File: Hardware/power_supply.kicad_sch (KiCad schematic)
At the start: 25 parts, among them J1 Conn_01x02_Pin, U1 MIC26903YJL-TR, U2 LD39200PU33R, U3 INA226AIDGSR

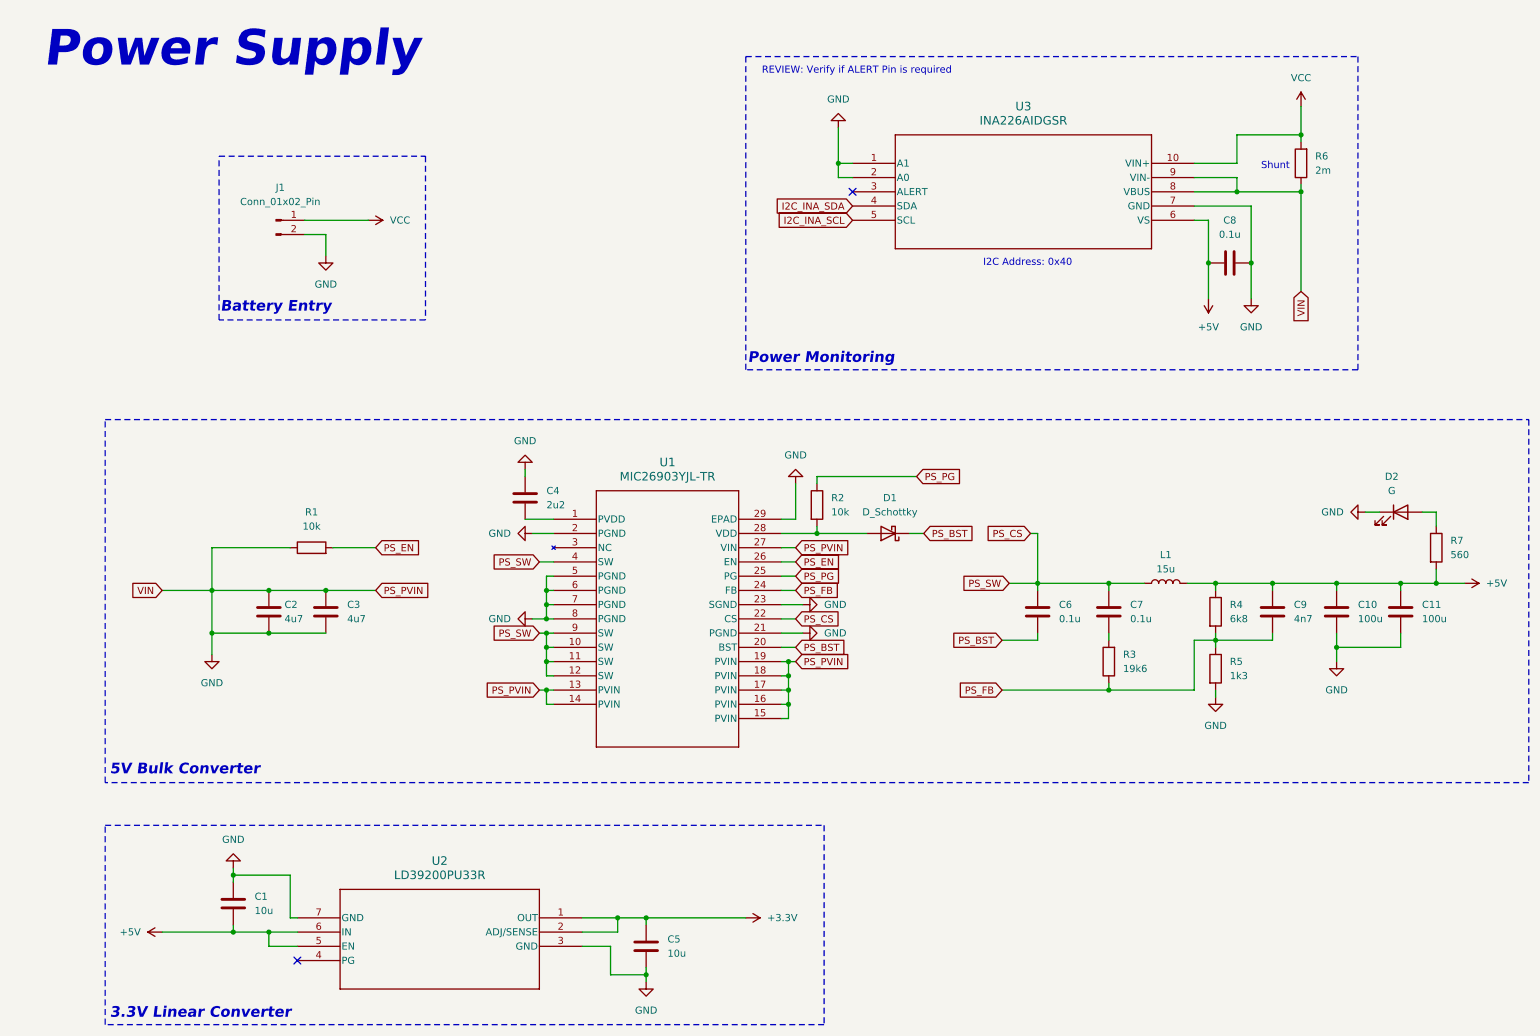
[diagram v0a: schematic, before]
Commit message: fcu, nu schematics, problem with pins
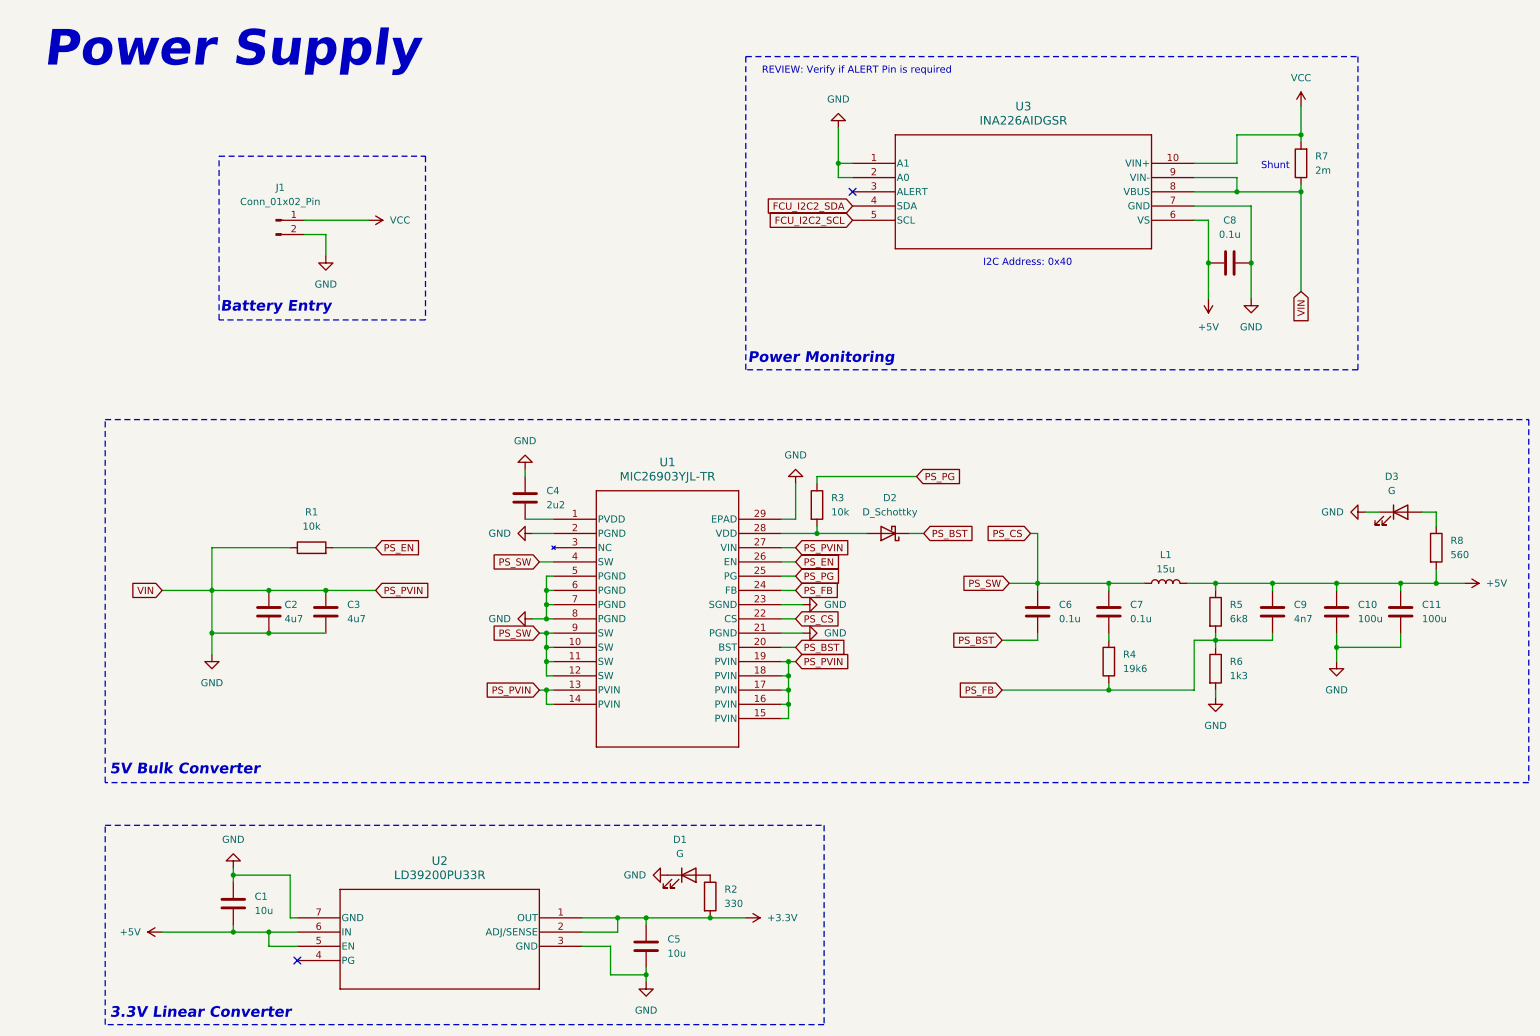
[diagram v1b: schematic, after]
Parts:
- added D1: G, symbol Device:LED
- added R2: 330, symbol Device:R
- renumbered D1 to D2, D2 to D3, R2 to R3, R3 to R4, R4 to R5, R5 to R6, R6 to R7, R7 to R8
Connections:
- net +3.3V: now also R2.2
- net GND: now also D1.1 (K)
- net I2C_INA_SCL renamed FCU_I2C2_SCL
- net I2C_INA_SDA renamed FCU_I2C2_SDA
- new net: D1.2 (A), R2.1

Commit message: version 0.1.0
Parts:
- removed C8: 0.1u, symbol Device:C
- removed R7: 2m, symbol Device:R
- removed U3: INA226AIDGSR, DGS10, symbol Aircraft_Components:INA226AIDGSR
- added C7: 100n, symbol Device:C
- added R2: 2m, symbol Device:R
- added U3: INA226, Aircraft_Footprints:DGS10, symbol Sensor_Energy:INA226
- renumbered C2 to C1, C3 to C2, C1 to C3, C7 to C8, R2 to R3, R3 to R4, R4 to R5, R5 to R6, R6 to R7
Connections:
- net +5V: now also C7.1, U3.6 (VS)
- net FCU_I2C2_SCL: now also U3.5 (SCL)
- net FCU_I2C2_SDA: now also U3.4 (SDA)
- net GND: now also C7.2, R2.1, U3.1 (A1), U3.2 (A0), U3.7 (GND), U3.8 (Vbus), U3.9 (Vin-)
- net VCC: now also R2.2, U3.10 (Vin+)
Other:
- note added: "3.3V Linear Regulator"
- note added: "5V Bulk Regulator"
- note added: "Circuit based on typical application in datasheet (need review)"
- note removed: "3.3V Linear Converter"
- note removed: "5V Bulk Converter"
- note removed: "I2C Address: 0x40"
- note removed: "Shunt"
- moved on the sheet: C1, C10, C11, C2, C3, C4, C5, C6, C8, C9, D1, D2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

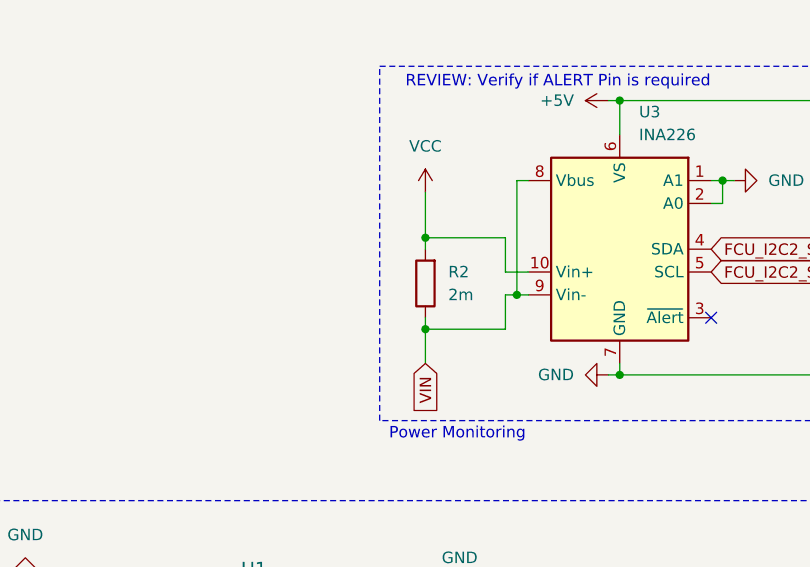
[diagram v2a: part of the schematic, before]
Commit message: version 0.1.1, added dfu usb to firmware upload, changed pwm channels
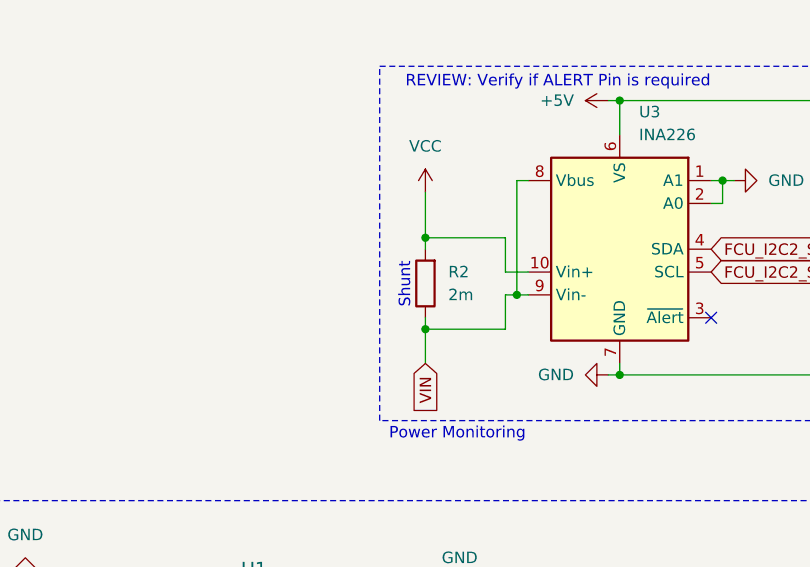
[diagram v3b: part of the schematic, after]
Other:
- note added: "Shunt"
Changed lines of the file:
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@@
+		)
+	)
+	(text "Shunt"
+		(exclude_from_sim no)
+		(at 141.224 52.324 90)
+		(effects
+			(font
+				(size 1.27 1.27)
+			)
 		)
 	)

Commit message: firmware started, freertos, initial sensors abstractions, some pin layout changes
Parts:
- U1: footprint MLF28_5X6_MCH -> (none)
- U2: footprint SON_DFN6_3X3_STM -> (none)
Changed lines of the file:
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@@
 			)
 		)
-		(property "Footprint" "MLF28_5X6_MCH"
+		(property "Footprint" ""
 			(at 104.14 93.98 0)
 			(effects
@@
 			)
 		)
-		(property "Footprint" "SON_DFN6_3X3_STM"
+		(property "Footprint" ""
 			(at 127 167.64 0)
 			(effects

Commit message: add some footprints, and pcb configs
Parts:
- C7: footprint (none) -> Capacitor_SMD:C_0603_1608Metric
- D1, D3: footprint (none) -> LED_SMD:LED_0603_1608Metric
- D2: footprint (none) -> Diode_SMD:D_SOD-323_HandSoldering
- R3, R8: footprint (none) -> Resistor_SMD:R_0603_1608Metric_Pad0.98x0.95mm_HandSolder
- U1: footprint (none) -> Aircraft_Footprints:MLF28_5X6_MCH
- U2: footprint (none) -> Aircraft_Footprints:SON_DFN6_3X3_STM
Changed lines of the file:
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@@
 		(dnp no)
 		(fields_autoplaced yes)
-		(property "Reference" "#PWR017"
+		(property "Reference" "#PWR019"
 			(at 222.25 132.08 0)
 			(effects
@@
 			(project ""
 				(path "/8dc22ddc-eb0a-4b80-a714-26a959e826d2/39a9e851-414a-49a1-b5c9-24c58b61cca2"
-					(reference "#PWR017")
+					(reference "#PWR019")
 					(unit 1)
 				)
@@
 			)
 		)
-		(property "Footprint" ""
+		(property "Footprint" "LED_SMD:LED_0603_1608Metric"
 			(at 255.27 92.71 0)
 			(effects
@@
 		(dnp no)
 		(fields_autoplaced yes)
-		(property "Reference" "#PWR019"
+		(property "Reference" "#PWR021"
 			(at 242.57 92.71 0)
 			(effects
@@
 			(project ""
 				(path "/8dc22ddc-eb0a-4b80-a714-26a959e826d2/39a9e851-414a-49a1-b5c9-24c58b61cca2"
-					(reference "#PWR019")
+					(reference "#PWR021")
 					(unit 1)
 				)
@@
 			)
 		)
-		(property "Footprint" ""
+		(property "Footprint" "Diode_SMD:D_SOD-323_HandSoldering"
 			(at 163.83 96.52 0)
 			(effects
@@
 		(dnp no)
 		(fields_autoplaced yes)
-		(property "Reference" "#PWR0112"
+		(property "Reference" "#PWR017"
 			(at 157.48 62.23 0)
 			(effects
@@
 			(project ""
 				(path "/8dc22ddc-eb0a-4b80-a714-26a959e826d2/39a9e851-414a-49a1-b5c9-24c58b61cca2"
-					(reference "#PWR0112")
+					(reference "#PWR017")
 					(unit 1)
 				)
@@
 			)
 		)
-		(property "Footprint" ""
+		(property "Footprint" "Resistor_SMD:R_0603_1608Metric_Pad0.98x0.95mm_HandSolder"
 			(at 259.842 99.06 90)
 			(effects
@@
 			)
 		)
-		(property "Footprint" ""
+		(property "Footprint" "Aircraft_Footprints:MLF28_5X6_MCH"
 			(at 104.14 93.98 0)
 			(effects
@@
 		(dnp no)
 		(fields_autoplaced yes)
-		(property "Reference" "#PWR020"
+		(property "Reference" "#PWR022"
 			(at 262.89 105.41 0)
 			(effects
@@
 			(project ""
 				(path "/8dc22ddc-eb0a-4b80-a714-26a959e826d2/39a9e851-414a-49a1-b5c9-24c58b61cca2"
-					(reference "#PWR020")
+					(reference "#PWR022")
 					(unit 1)
 				)
@@
 		(dnp no)
 		(fields_autoplaced yes)
-		(property "Reference" "#PWR018"
+		(property "Reference" "#PWR020"
 			(at 243.84 125.73 0)
 			(effects
@@
 			(project ""
 				(path "/8dc22ddc-eb0a-4b80-a714-26a959e826d2/39a9e851-414a-49a1-b5c9-24c58b61cca2"
-					(reference "#PWR018")
+					(reference "#PWR020")
 					(unit 1)
 				)
@@
 			)
 		)
-		(property "Footprint" ""
+		(property "Footprint" "Capacitor_SMD:C_0603_1608Metric"
 			(at 195.2752 52.07 0)
 			(effects
@@
 		(dnp no)
 		(fields_autoplaced yes)
-		(property "Reference" "#PWR0111"
+		(property "Reference" "#PWR016"
 			(at 167.64 31.75 0)
 			(effects
@@
 			(project ""
 				(path "/8dc22ddc-eb0a-4b80-a714-26a959e826d2/39a9e851-414a-49a1-b5c9-24c58b61cca2"
-					(reference "#PWR0111")
+					(reference "#PWR016")
 					(unit 1)
 				)
@@
 		(dnp no)
 		(fields_autoplaced yes)
-		(property "Reference" "#PWR016"
+		(property "Reference" "#PWR018"
 			(at 184.15 40.64 0)
 			(effects
@@
 			(project ""
 				(path "/8dc22ddc-eb0a-4b80-a714-26a959e826d2/39a9e851-414a-49a1-b5c9-24c58b61cca2"
-					(reference "#PWR016")
+					(reference "#PWR018")
 					(unit 1)
 				)
@@
 			)
 		)
-		(property "Footprint" ""
+		(property "Footprint" "LED_SMD:LED_0603_1608Metric"
 			(at 146.05 160.02 0)
 			(effects
@@
 			)
 		)
-		(property "Footprint" ""
+		(property "Footprint" "Resistor_SMD:R_0603_1608Metric_Pad0.98x0.95mm_HandSolder"
 			(at 148.082 163.83 90)
 			(effects
@@
 			)
 		)
-		(property "Footprint" ""
+		(property "Footprint" "Aircraft_Footprints:SON_DFN6_3X3_STM"
 			(at 127 167.64 0)
 			(effects
